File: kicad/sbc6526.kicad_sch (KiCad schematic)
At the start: 0 parts

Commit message: v2.0
Production ready
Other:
- company: (none) -> Daniel Molina García
- title: (none) -> SBC6526 - Block Diagram
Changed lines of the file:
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@@
 (kicad_sch (version 20201015) (generator eeschema)
   (paper "A4")
+  (title_block
+    (title "SBC6526 - Block Diagram")
+    (date "2021-10-01")
+    (rev "2.0")
+    (company "Daniel Molina García")
+  )
   (junction (at 130.81 73.66) (diameter 1.016) (color 0 0 0 0))
   (junction (at 130.81 100.33) (diameter 1.016) (color 0 0 0 0))

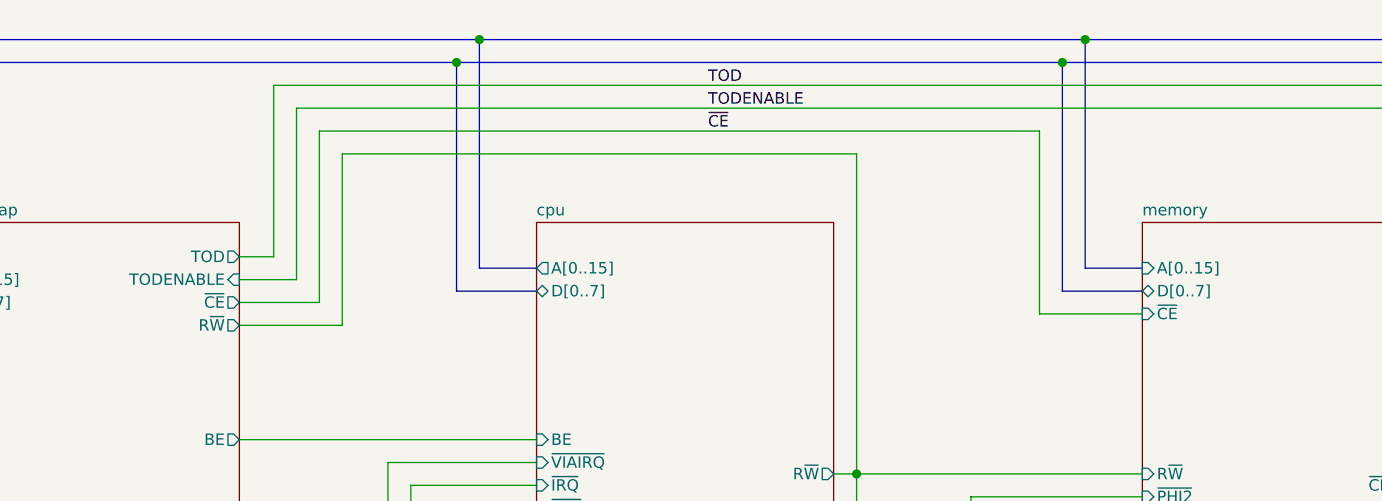
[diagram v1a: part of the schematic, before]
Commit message: Fixes
* Minor fixes to routing
* Right VCC hole was slightly offset. Fixed
* Removed /CE from arduino to RAM. As RAMCE pulses with PHI, it's not necessary, and we leave /CE tied to GND.
* Fixed RAM footprint, as it was too wide. Improved routing.
* Added current limiting resistor to LCD Contrast
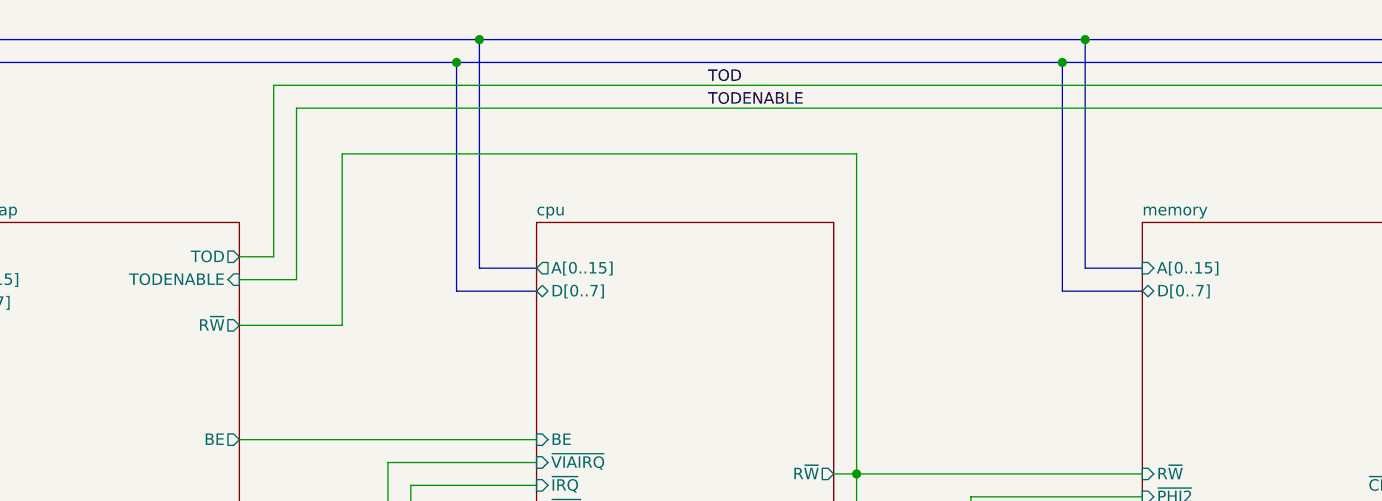
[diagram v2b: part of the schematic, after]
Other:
- sheet bootstrap ports: added none; removed ~CE
- sheet memory ports: added none; removed ~CE
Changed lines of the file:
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@@
-    (stroke (width 0) (type solid) (color 0 0 0 0))
-  )
-  (wire (pts (xy 62.23 54.61) (xy 71.12 54.61))
     (stroke (width 0) (type solid) (color 0 0 0 0))
   )
@@
     (stroke (width 0) (type solid) (color 0 0 0 0))
   )
-  (wire (pts (xy 71.12 35.56) (xy 71.12 54.61))
-    (stroke (width 0) (type solid) (color 0 0 0 0))
-  )
   (wire (pts (xy 73.66 38.1) (xy 73.66 57.15))
     (stroke (width 0) (type solid) (color 0 0 0 0))
@@
   )
   (wire (pts (xy 146.05 124.46) (xy 146.05 97.79))
-    (stroke (width 0) (type solid) (color 0 0 0 0))
-  )
-  (wire (pts (xy 151.13 35.56) (xy 71.12 35.56))
-    (stroke (width 0) (type solid) (color 0 0 0 0))
-  )
-  (wire (pts (xy 151.13 55.88) (xy 151.13 35.56))
-    (stroke (width 0) (type solid) (color 0 0 0 0))
-  )
-  (wire (pts (xy 162.56 55.88) (xy 151.13 55.88))
     (stroke (width 0) (type solid) (color 0 0 0 0))
   )
@@
   )
   (label "TODENABLE" (at 114.3 33.02 0)
-    (effects (font (size 1.27 1.27)) (justify left bottom))
-  )
-  (label "~CE" (at 114.3 35.56 0)
     (effects (font (size 1.27 1.27)) (justify left bottom))
   )
@@
       (effects (font (size 1.27 1.27)) (justify right))
     )
-    (pin "~CE" output (at 62.23 54.61 0)
-      (effects (font (size 1.27 1.27)) (justify right))
-    )
     (pin "R~W" output (at 62.23 57.15 0)
       (effects (font (size 1.27 1.27)) (justify right))
@@
     (pin "~VIA" output (at 195.58 72.39 0)
       (effects (font (size 1.27 1.27)) (justify right))
-    )
-    (pin "~CE" input (at 162.56 55.88 180)
-      (effects (font (size 1.27 1.27)) (justify left))
     )
     (pin "R~W" input (at 162.56 73.66 180)
@@
       (reference "R10") (unit 1) (value "330") (footprint "Resistor_SMD:R_0805_2012Metric_Pad1.20x1.40mm_HandSolder")
     )
+    (path "/00000000-0000-0000-0000-00005fa75ce1/c089f098-3c93-481b-9af1-e975d87219d5"
+      (reference "R20") (unit 1) (value "1k") (footprint "Resistor_SMD:R_0805_2012Metric_Pad1.20x1.40mm_HandSolder")
+    )
     (path "/00000000-0000-0000-0000-00005fa75ce1/00000000-0000-0000-0000-00005fa7774d"

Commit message: Uploaded firmware v2.0.2
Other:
- sheet bootstrap ports: added R~{W}; removed R~W
- sheet clock ports: added ~{PHI2}; removed ~PHI2
- sheet clockmeter ports: added ~{PHI2}; removed ~PHI2
- sheet cpu ports: added R~{W}, ~{IRQ}, ~{RES}, ~{VIAIRQ}; removed R~W, ~IRQ, ~RES, ~VIAIRQ
- sheet memory ports: added R~{W}, ~{CIAEXT}, ~{CIA}, ~{PHI2}, ~{VIA}; removed R~W, ~CIA, ~CIAEXT, ~PHI2, ~VIA
- sheet peripherals ports: added R~{W}, ~{CIAEXT}, ~{CIA}, ~{IRQ}, ~{RES}, ~{VIAIRQ}, ~{VIA}; removed R~W, ~CIA, ~CIAEXT, ~IRQ, ~RES, ~VIA, ~VIAIRQ
- sheet reset ports: added ~{RES}; removed ~RES

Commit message: PullUps con SERCLOCK and SERDAT
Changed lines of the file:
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@@
-    (stroke (width 0) (type solid) (color 0 0 0 0))
-  )
-  (bus (pts (xy 276.86 137.16) (xy 259.08 137.16))
     (stroke (width 0) (type solid) (color 0 0 0 0))
   )
@@
     (stroke (width 0) (type solid) (color 0 0 0 0))
   )
+  (bus (pts (xy 259.08 137.16) (xy 276.86 137.16))
+    (stroke (width 0) (type default) (color 0 0 0 0))
+  )
   (wire (pts (xy 68.58 33.02) (xy 68.58 52.07))
     (stroke (width 0) (type solid) (color 0 0 0 0))
@@
     (stroke (width 0) (type solid) (color 0 0 0 0))
   )
+  (wire (pts (xy 143.51 76.2) (xy 143.51 127))
+    (stroke (width 0) (type solid) (color 0 0 0 0))
+  )
+  (wire (pts (xy 66.04 49.53) (xy 66.04 30.48))
+    (stroke (width 0) (type solid) (color 0 0 0 0))
+  )
+  (wire (pts (xy 64.77 82.55) (xy 64.77 123.19))
+    (stroke (width 0) (type solid) (color 0 0 0 0))
+  )
   (bus (pts (xy 265.43 88.9) (xy 276.86 88.9))
-    (stroke (width 0) (type solid) (color 0 0 0 0))
-  )
-  (wire (pts (xy 143.51 76.2) (xy 143.51 127))
-    (stroke (width 0) (type solid) (color 0 0 0 0))
-  )
-  (wire (pts (xy 66.04 49.53) (xy 66.04 30.48))
-    (stroke (width 0) (type solid) (color 0 0 0 0))
-  )
-  (wire (pts (xy 64.77 82.55) (xy 64.77 123.19))
-    (stroke (width 0) (type solid) (color 0 0 0 0))
+    (stroke (width 0) (type default) (color 0 0 0 0))
   )
   (bus (pts (xy 95.25 53.34) (xy 86.36 53.34))
@@
       (reference "#PWR02") (unit 1) (value "VCC") (footprint "")
     )
+    (path "/00000000-0000-0000-0000-00005fa75ce1/18c0bcb6-b0de-425a-9e6e-f50e9332b6dd"
+      (reference "#PWR03") (unit 1) (value "VCC") (footprint "")
+    )
     (path "/00000000-0000-0000-0000-00005fa7ba55/00000000-0000-0000-0000-00005fad6588"
       (reference "#PWR0101") (unit 1) (value "GND") (footprint "")
@@
       (reference "R20") (unit 1) (value "1k") (footprint "Resistor_SMD:R_0805_2012Metric_Pad1.20x1.40mm_HandSolder")
     )
+    (path "/00000000-0000-0000-0000-00005fa75ce1/e2debc15-c16a-4456-93cc-3069d0c14761"
+      (reference "R21") (unit 1) (value "3k3") (footprint "Resistor_SMD:R_0805_2012Metric_Pad1.20x1.40mm_HandSolder")
+    )
+    (path "/00000000-0000-0000-0000-00005fa75ce1/d897c21c-f312-4d4e-9a00-c62704dfa6c1"
+      (reference "R22") (unit 1) (value "3k3") (footprint "Resistor_SMD:R_0805_2012Metric_Pad1.20x1.40mm_HandSolder")
+    )
     (path "/00000000-0000-0000-0000-00005fb72ec4/00000000-0000-0000-0000-00005ff85c1a"
